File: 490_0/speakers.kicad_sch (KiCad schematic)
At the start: 5 parts, among them J1 S2B-XH-A, U1 MAX98357A

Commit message: Changed 8conn and BOM update
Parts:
- C1: footprint (none) -> Capacitor_SMD:C_1206_3216Metric
- C2: footprint (none) -> Capacitor_SMD:C_0805_2012Metric
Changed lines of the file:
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@@
 			)
 		)
-		(property "Footprint" ""
+		(property "Footprint" "Capacitor_SMD:C_0805_2012Metric"
 			(at 108.9152 69.85 0)
 			(effects
@@
 			)
 		)
-		(property "Footprint" ""
+		(property "Footprint" "Capacitor_SMD:C_1206_3216Metric"
 			(at 100.6348 69.85 0)
 			(effects

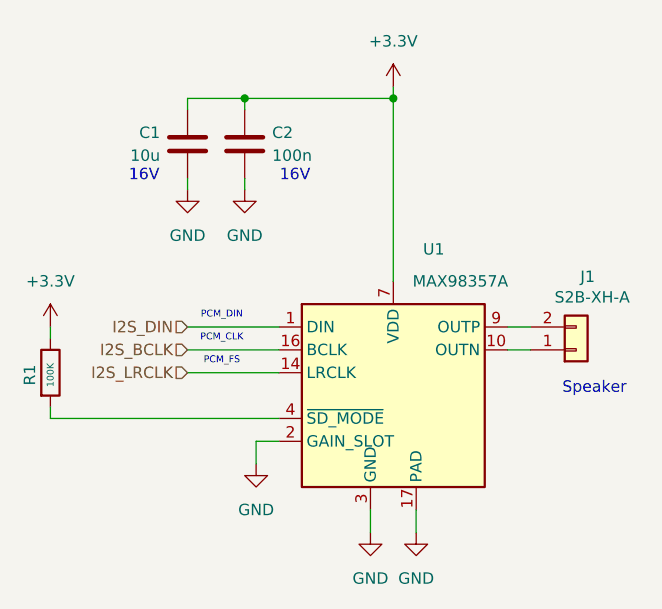
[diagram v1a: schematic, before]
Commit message: Fixed capacitor symbols
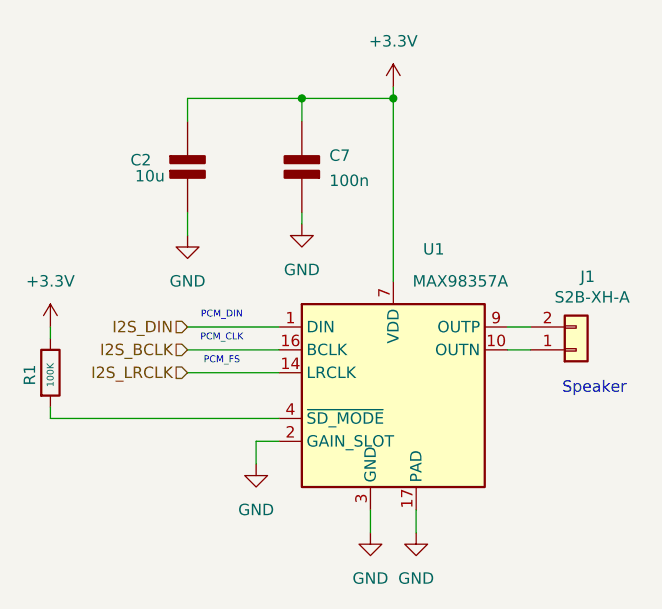
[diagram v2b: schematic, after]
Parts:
- removed C1: 10u, Capacitor_SMD:C_1206_3216Metric, symbol Device:C
- removed C2: 100n, Capacitor_SMD:C_0805_2012Metric, symbol Device:C
- added C2: 10u, Capacitor_SMD:C_1206_3216Metric, symbol PCM_Elektuur:C
- added C7: 100n, Capacitor_SMD:C_0805_2012Metric, symbol PCM_Elektuur:C
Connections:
- net +3.3V: now also C2.1 (+), C7.2 (-)
- net GND: now also C2.2 (-), C7.1 (+)
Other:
- note removed: "16V"

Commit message: PCB Jumpstart
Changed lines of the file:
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@@
 	)
 	(hierarchical_label "I2S_DIN"
-		(shape input)
+		(shape bidirectional)
 		(at 101.6 86.36 180)
 		(effects
@@
 	)
 	(hierarchical_label "I2S_BCLK"
-		(shape input)
+		(shape bidirectional)
 		(at 101.6 88.9 180)
 		(effects
@@
 	)
 	(hierarchical_label "I2S_LRCLK"
-		(shape input)
+		(shape bidirectional)
 		(at 101.6 91.44 180)
 		(effects

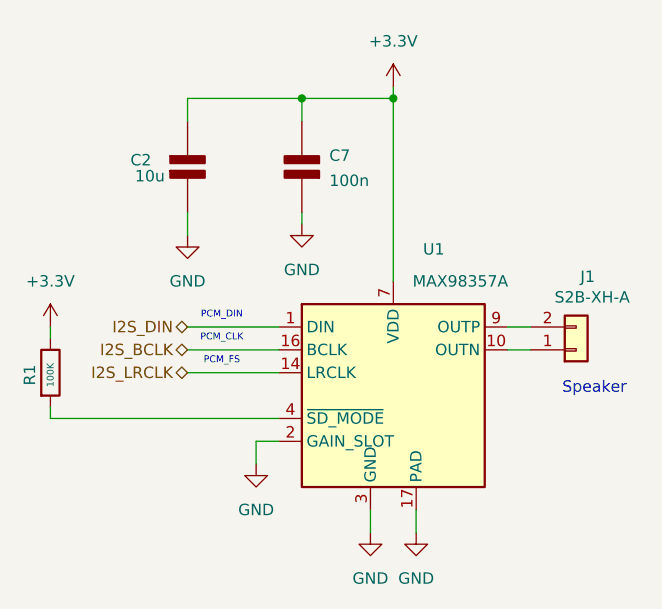
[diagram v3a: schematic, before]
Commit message: Changed footprints for pad connectors (for soldered components)
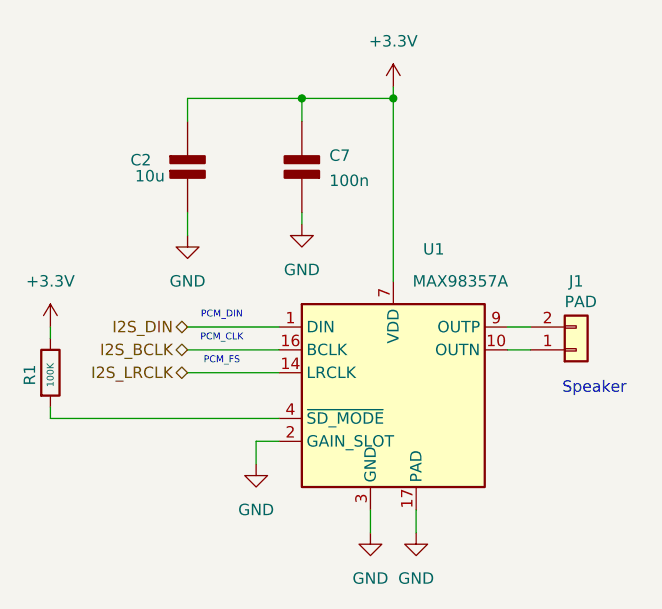
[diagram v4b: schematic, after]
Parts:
- J1: value S2B-XH-A -> PAD; footprint *CapStone*:JST_S2B-XH-A -> Connector_PinHeader_1.27mm:PinHeader_1x02_P1.27mm_Vertical
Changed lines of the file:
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@@
 		(dnp no)
 		(property "Reference" "J1"
-			(at 146.05 80.772 0)
+			(at 144.78 81.28 0)
 			(effects
 				(font
@@
 			)
 		)
-		(property "Value" "S2B-XH-A"
-			(at 146.558 83.058 0)
+		(property "Value" "PAD"
+			(at 145.288 83.566 0)
 			(effects
 				(font
@@
 			)
 		)
-		(property "Footprint" "*CapStone*:JST_S2B-XH-A"
+		(property "Footprint" "Connector_PinHeader_1.27mm:PinHeader_1x02_P1.27mm_Vertical"
 			(at 144.145 93.345 0)
 			(effects

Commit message: Changed capacitor sizes
🟢 Group 1: 100% Safe to Shrink to 0603These capacitors handle logic-level decoupling or high-frequency filtering on your 3.3V and 5V lines. Because the capacitance values are low (1µF or less), an 0603 package can easily handle the DC bias without losing performance.All 0.1µF (100nF) Capacitors: You have 25 of these scattered across the board (e.g., C35, C41, C42, C49, C53-C61). Change every single one of these to 0603.The 1µF Logic Capacitors (C48, C62): C48 sits on the VCC pin of your battery charger. C62 is on the 3.3V rail for the USB hub. Change these to 0603.The 4.7µF Capacitors (C45, C47, C50): C45 and C47 sit on the 5V VL pin. C50 filters the 5V HDMI line. Change these to 0603.The 33pF Capacitors (C17, C18, C36): C17 and C18 are your crystal load capacitors and are already perfectly sized. C36 is a feedforward capacitor for your buck converter. Make sure all three are 0603.
🟡 Group 2: The "Compromise" - Shrink to 0805These 10µF capacitors sit on your 5V and 3.3V rails to smooth out the power for your motors, speakers, and USB hub (e.g., C1, C2, C4, C6, C12, C13, C15, C20, C22, C24).The Recommendation: While you have them listed as 1206, shrinking a 10µF ceramic capacitor all the way down to 0603 for a noisy 5V motor line will cause it to lose too much effective capacitance. 0805 is the perfect middle-ground here. It saves space but keeps your motor rails stable.
🔴 Group 3: DO NOT SHRINK (Keep 1206 / 1210 / 2824)These capacitors are exposed to the +VBATT_7V4 rail (up to 8.4V) or act as massive bulk storage. If you shrink these, your system will likely fail under heavy load.C32, C33, C34 (10µF): These connect directly to the high-voltage VIN pin of your main buck converter. Keep as 1206.C44 (22µF): This is the main switching capacitor for the battery charger inductor. Keep as 1210.C37, C38, C39, C40, C46 (22µF): These are the massive bulk output capacitors holding up your main 5V rail. Keep as 1210.C43 (1µF): Because this sits on the VH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
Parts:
- C2: Digikey Link https://www.digikey.ca/en/products/detail/kemet/c1206c106k4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 -> https://www.digikey.ca/en/products/detail/samsung-electro-m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; Manufacturer KEMET -> Samsung Electro-Mechanics; Manufacturer Part C1206C106K4RACTU -> CL21B106KOQNNNE; Package 1206 (3216 Metric) -> 0805; Price 0.31 -> 0.22; Supplier P/N 399-C1206C106K4RACTUCT-ND -> 1276-2872-1-ND
- C7: Digikey Link https://www.digikey.ca/en/products/detail/yageo/CC0805KRX7R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 -> https://www.digikey.ca/en/products/detail/yageo/CC0603KRX7R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; Manufacturer Part CC0805KRX7R9BB104 -> CC0603KRX7R9BB104; Package 0805 (2012 Metric) -> 0603 (1608 Metric); Supplier P/N 311-1140-1-ND -> 311-1344-1-ND
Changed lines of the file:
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@@
 			)
 		)
-		(property "Description" "CAP CER 0.1UF 50V X7R 0805"
+		(property "Description" "CAP CER 0.1UF 50V X7R 0603"
 			(at 114.3 68.58 0)
 			(effects
@@
 			)
 		)
-		(property "Digikey Link" "https://www.digikey.ca/en/products/detail/yageo/CC0805KRX7R9BB104/302874?s=N4IgTCBcDaIMJwAwA5EFYDSAlAGgdiwE4AhYgRkQBYQBdAXyA"
+		(property "Digikey Link" "https://www.digikey.ca/en/products/detail/yageo/CC0603KRX7R9BB104/2103082"
 			(at 114.3 68.58 0)
 			(effects
@@
 			)
 		)
-		(property "Manufacturer Part" "CC0805KRX7R9BB104"
+		(property "Manufacturer Part" "CC0603KRX7R9BB104"
 			(at 114.3 68.58 0)
 			(effects
@@
 			)
 		)
-		(property "Package" "0805 (2012 Metric)"
+		(property "Package" "0603 (1608 Metric)"
 			(at 114.3 68.58 0)
 			(effects
@@
 			)
 		)
-		(property "Supplier P/N" "311-1140-1-ND"
+		(property "Supplier P/N" "311-1344-1-ND"
 			(at 114.3 68.58 0)
 			(effects
@@
 			)
 		)
-		(property "Datasheet" "kicad-embed://KEM_C1002_X7R_SMD.pdf"
-			(at 101.6 68.58 0)
-			(effects
-				(font
-					(size 1.27 1.27)
-				)
-				(hide yes)
-			)
-		)
-		(property "Description" "CAP CER 10UF 16V X7R 1206"
+		(property "Datasheet" "kicad-embed://CL_Series_MLCC_ds.pdf"
+			(at 101.6 68.58 0)
+			(effects
+				(font
+					(size 1.27 1.27)
+				)
+				(hide yes)
+			)
+		)
+		(property "Description" "CAP CER 10UF 16V X7R 0805"
 			(at 101.6 68.58 0)
 			(effects
@@
 			)
 		)
-		(property "Digikey Link" "https://www.digikey.ca/en/products/detail/kemet/c1206c106k4ractu/789657"
+		(property "Digikey Link" "https://www.digikey.ca/en/products/detail/samsung-electro-mechanics/CL21B106KOQNNNE/3888530"
 			(at 101.6 68.58 0)
 			(effects
@@
 			)
 		)
-		(property "Manufacturer" "KEMET"
+		(property "Manufacturer" "Samsung Electro-Mechanics"
 			(at 101.6 68.58 0)
 			(effects
@@
 			)
 		)
-		(property "Manufacturer Part" "C1206C106K4RACTU"
+		(property "Manufacturer Part" "CL21B106KOQNNNE"
 			(at 101.6 68.58 0)
 			(effects
@@
 			)
 		)
-		(property "Supplier P/N" "399-C1206C106K4RACTUCT-ND"
+		(property "Supplier P/N" "1276-2872-1-ND"
 			(at 101.6 68.58 0)
 			(effects
@@
 			)
 		)
-		(property "Package" "1206 (3216 Metric)"
-			(at 101.6 68.58 0)
-			(effects
-				(font
-					(size 1.27 1.27)
-				)
-				(hide yes)
-			)
-		)
-		(property "Price" "0.31"
-			(at 101.6 68.58 0)
-			(effects
+		(property "Package" "0805"
+			(at 101.6 68.58 0)
+			(effects
+				(font
+					(size 1.27 1.27)
+				)
+				(hide yes)
+			)
+		)
+		(property "Price" "0.22"
+			(at 101.6 68.58 0)
+			(effects

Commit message: Assigned capacitor footprints
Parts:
- C2: footprint Capacitor_SMD:C_1206_3216Metric -> Capacitor_SMD:C_0805_2012Metric
- C7: footprint Capacitor_SMD:C_0805_2012Metric -> Capacitor_SMD:C_0603_1608Metric
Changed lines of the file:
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@@
 			)
 		)
-		(property "Footprint" "Capacitor_SMD:C_0805_2012Metric"
+		(property "Footprint" "Capacitor_SMD:C_0603_1608Metric"
 			(at 114.3 68.58 0)
 			(effects
@@
 			)
 		)
-		(property "Footprint" "Capacitor_SMD:C_1206_3216Metric"
+		(property "Footprint" "Capacitor_SMD:C_0805_2012Metric"
 			(at 101.6 68.58 0)
 			(effects

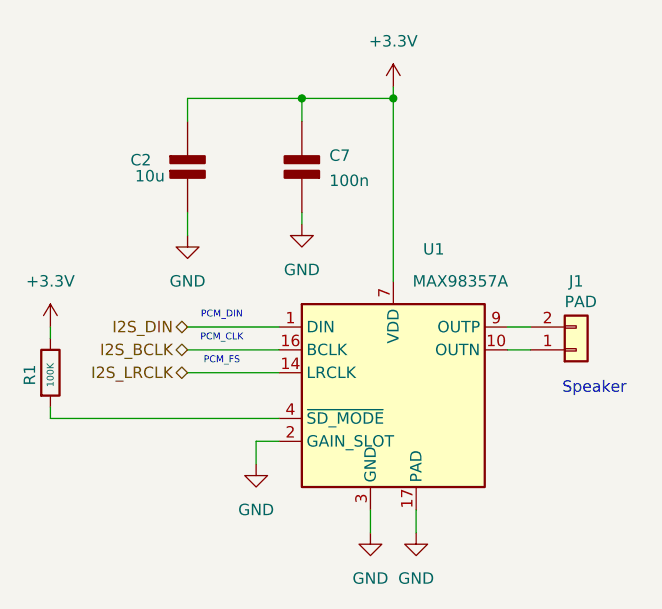
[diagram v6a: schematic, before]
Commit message: Changed all the resistors to 0805 size
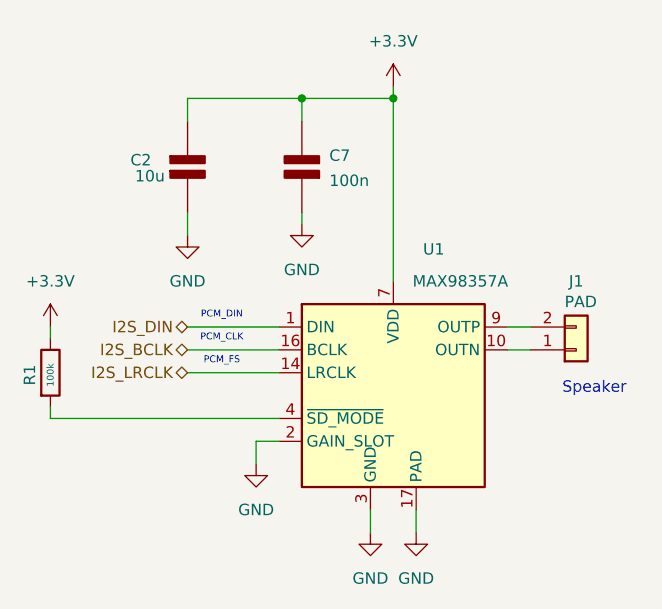
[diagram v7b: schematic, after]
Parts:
- R1: value 100K -> 100k; footprint Resistor_SMD:R_0603_1608Metric -> Resistor_SMD:R_0805_2012Metric; Digikey Link https://www.digikey.ca/en/products/detail/yageo/RC1206FR-07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 -> https://www.digikey.ca/en/products/detail/yageo/RC0805FR-07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; Manufacturer Part RC1206FR-07100KL -> RC0805FR-07100KL; Package 1206 -> 0805; Supplier P/N 311-100KFRCT-ND -> 311-100KCRCT-ND
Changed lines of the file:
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@@
 			)
 		)
-		(property "Value" "100K"
+		(property "Value" "100k"
 			(at 86.36 91.694 90)
 			(effects
@@
 			)
 		)
-		(property "Footprint" "Resistor_SMD:R_0603_1608Metric"
+		(property "Footprint" "Resistor_SMD:R_0805_2012Metric"
 			(at 84.582 91.44 90)
 			(effects
@@
 			)
 		)
-		(property "Datasheet" "kicad-embed://PYU-RC_GROUP_51_ROHS_L (YAGEO resistors).pdf"
+		(property "Datasheet" "kicad-embed://RC0805FR-07100KL (100k ohm resistor).pdf"
 			(at 86.36 91.44 0)
 			(effects
@@
 			)
 		)
-		(property "Description" "RES 100K OHM 1% 1/4W 1206"
+		(property "Description" "RES 100K OHM 1% 1/8W 0805"
 			(at 86.36 91.44 0)
 			(effects
@@
 			)
 		)
-		(property "Digikey Link" "https://www.digikey.ca/en/products/detail/yageo/RC1206FR-07100KL/728492"
+		(property "Digikey Link" "https://www.digikey.ca/en/products/detail/yageo/RC0805FR-07100KL/727544"
 			(at 86.36 91.44 90)
 			(effects
@@
 			)
 		)
-		(property "Manufacturer Part" "RC1206FR-07100KL"
+		(property "Manufacturer Part" "RC0805FR-07100KL"
 			(at 86.36 91.44 90)
 			(effects
@@
 			)
 		)
-		(property "Supplier P/N" "311-100KFRCT-ND"
+		(property "Supplier P/N" "311-100KCRCT-ND"
 			(at 86.36 91.44 90)
 			(effects
@@
 			)
 		)
-		(property "Package" "1206"
-			(at 86.36 91.44 90)
-			(effects
+		(property "Package" "0805"
+			(at 86.36 91.44 90)
+			(effects

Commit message: Changed audio chip to 5V
It might pull to omuch if we ue the raspberry's 3.3V rail
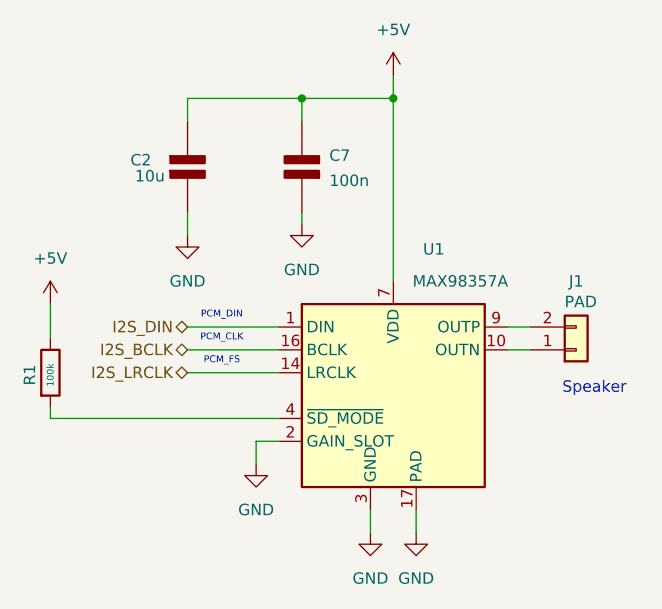
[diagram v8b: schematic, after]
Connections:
- net +3.3V renamed +5V
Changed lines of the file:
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@@
 	(wire
 		(pts
-			(xy 86.36 86.36) (xy 86.36 87.63)
+			(xy 86.36 83.82) (xy 86.36 87.63)
 		)
 		(stroke
@@
 	(wire
 		(pts
-			(xy 124.46 59.69) (xy 124.46 60.96)
+			(xy 124.46 58.42) (xy 124.46 60.96)
 		)
 		(stroke
@@
 	)
 	(symbol
-		(lib_id "power:+5V")
-		(at 124.46 59.69 0)
-		(unit 1)
-		(exclude_from_sim no)
-		(in_bom yes)
-		(on_board yes)
-		(dnp no)
-		(fields_autoplaced yes)
-		(property "Reference" "#PWR01"
-			(at 124.46 63.5 0)
-			(effects
-				(font
-					(size 1.27 1.27)
-				)
-				(hide yes)
-			)
-		)
-		(property "Value" "+3.3V"
-			(at 124.46 54.61 0)
-			(effects
-				(font
-					(size 1.27 1.27)
-				)
-			)
-		)
-		(property "Footprint" ""
-			(at 124.46 59.69 0)
-			(effects
-				(font
-					(size 1.27 1.27)
-				)
-				(hide yes)
-			)
-		)
-		(property "Datasheet" ""
-			(at 124.46 59.69 0)
-			(effects
-				(font
-					(size 1.27 1.27)
-				)
-				(hide yes)
-			)
-		)
-		(property "Description" "Power symbol creates a global label with name \"+5V\""
-			(at 124.46 59.69 0)
-			(effects
-				(font
-					(size 1.27 1.27)
-				)
-				(hide yes)
-			)
-		)
-		(pin "1"
-		)
-		(instances
-			(project "490_0"
-				(path "/365a82ed-827d-43e1-aa2f-b98221c4179c/f9f22bb2-829e-4ff5-89be-c4b5e2122135/53573971-fb61-48df-903f-f9c3fbfa6843"
-					(reference "#PWR01")
-					(unit 1)
-				)
-			)
-		)
-	)
-	(symbol
 		(lib_id "power:GND")
 		(at 101.6 76.2 0)
@@
 	)
 	(symbol
+		(lib_id "power:+3.3V")
+		(at 86.36 83.82 0)
+		(mirror y)
+		(unit 1)
+		(exclude_from_sim no)
+		(in_bom yes)
+		(on_board yes)
+		(dnp no)
+		(fields_autoplaced yes)
+		(property "Reference" "#PWR04"
+			(at 86.36 87.63 0)
+			(effects
+				(font
+					(size 1.27 1.27)
+				)
+				(hide yes)
+			)
+		)
+		(property "Value" "+5V"
+			(at 86.36 78.74 0)
+			(effects
+				(font
+					(size 1.27 1.27)
+				)
+			)
+		)
+		(property "Footprint" ""
+			(at 86.36 83.82 0)
+			(effects
+				(font
+					(size 1.27 1.27)
+				)
+				(hide yes)
+			)
+		)
+		(property "Datasheet" ""
+			(at 86.36 83.82 0)
+			(effects
+				(font
+					(size 1.27 1.27)
+				)
+				(hide yes)
+			)
+		)
+		(property "Description" "Power symbol creates a global label with name \"+3.3V\""
+			(at 86.36 83.82 0)
+			(effects
+				(font
+					(size 1.27 1.27)
+				)
+				(hide yes)
+			)
+		)
+		(pin "1"
+		)
+		(instances
+			(project "490_0"
+				(path "/365a82ed-827d-43e1-aa2f-b98221c4179c/f9f22bb2-829e-4ff5-89be-c4b5e2122135/53573971-fb61-48df-903f-f9c3fbfa6843"
+					(reference "#PWR04")
+					(unit 1)
+				)
+			)
+		)
+	)
+	(symbol
 		(lib_id "Device:R")
 		(at 86.36 91.44 0)
@@
 				(path "/365a82ed-827d-43e1-aa2f-b98221c4179c/f9f22bb2-829e-4ff5-89be-c4b5e2122135/53573971-fb61-48df-903f-f9c3fbfa6843"
 					(reference "C2")
-					(unit 1)
-				)
-			)
-		)
-	)
-	(symbol
-		(lib_id "power:+5V")
-		(at 86.36 86.36 0)
-		(unit 1)
-		(exclude_from_sim no)
-		(in_bom yes)
-		(on_board yes)
-		(dnp no)
-		(fields_autoplaced yes)
-		(property "Reference" "#PWR04"
-			(at 86.36 90.17 0)
-			(effects
-				(font
-					(size 1.27 1.27)
-				)
-				(hide yes)
-			)
-		)
-		(property "Value" "+3.3V"
-			(at 86.36 81.28 0)
-			(effects
-				(font
-					(size 1.27 1.27)
-				)
-			)
-		)
-		(property "Footprint" ""
-			(at 86.36 86.36 0)
-			(effects
-				(font
-					(size 1.27 1.27)
-				)
-				(hide yes)
-			)
-		)
-		(property "Datasheet" ""
-			(at 86.36 86.36 0)
-			(effects
-				(font
-					(size 1.27 1.27)
-				)
-				(hide yes)
-			)
-		)
-		(property "Description" "Power symbol creates a global label with name \"+5V\""
-			(at 86.36 86.36 0)
-			(effects
-				(font
-					(size 1.27 1.27)
-				)
-				(hide yes)
-			)
-		)
-		(pin "1"
-		)
-		(instances
-			(project "490_0"
-				(path "/365a82ed-827d-43e1-aa2f-b98221c4179c/f9f22bb2-829e-4ff5-89be-c4b5e2122135/53573971-fb61-48df-903f-f9c3fbfa6843"
-					(reference "#PWR04")
 					(unit 1)
 				)
@@
 					(unit 1)
 				)
+			)
+		)
+	)
+	(symbol
+		(lib_id "power:+3.3V")
+		(at 124.46 58.42 0)
+		(mirror y)
+		(unit 1)
+		(exclude_from_sim no)
+		(in_bom yes)
+		(on_board yes)
+		(dnp no)
+		(fields_autoplaced yes)
+		(property "Reference" "#PWR01"
+			(at 124.46 62.23 0)
+			(effects
+				(font
+					(size 1.27 1.27)
+				)
+				(hide yes)
+			)
+		)
+		(property "Value" "+5V"
+			(at 124.46 53.34 0)
+			(effects
+				(font
+					(size 1.27 1.27)
+				)
+			)
+		)
+		(property "Footprint" ""
+			(at 124.46 58.42 0)
+			(effects
+				(font
+					(size 1.27 1.27)
+				)
+				(hide yes)
+			)
+		)
+		(property "Datasheet" ""
+			(at 124.46 58.42 0)
+			(effects
+				(font
+					(size 1.27 1.27)
+				)
+				(hide yes)
+			)
+		)
+		(property "Description" "Power symbol creates a global label with name \"+3.3V\""
+			(at 124.46 58.42 0)
+			(effects
+				(font
+					(size 1.27 1.27)
+				)
+				(hide yes)
+			)
+		)
+		(pin "1"
+		)
+		(instances
+			(project "490_0"
+				(path "/365a82ed-827d-43e1-aa2f-b98221c4179c/f9f22bb2-829e-4ff5-89be-c4b5e2122135/53573971-fb61-48df-903f-f9c3fbfa6843"
+					(reference "#PWR01")
+					(unit 1)
+				)
